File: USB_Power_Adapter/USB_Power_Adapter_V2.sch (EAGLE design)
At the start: 6 parts, among them J1 MICROUSBMICROUSB_THRU, U1 SC189

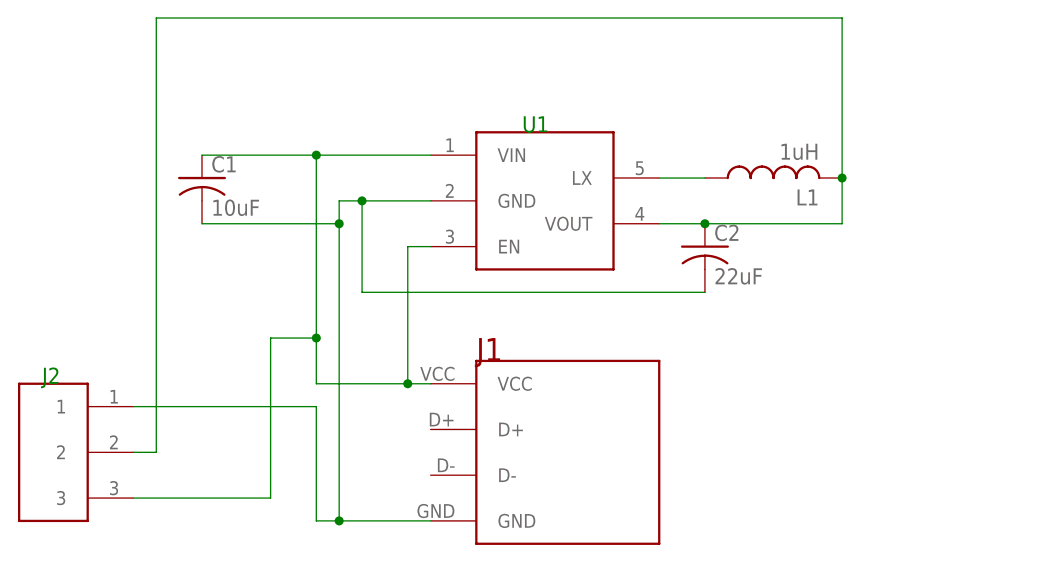
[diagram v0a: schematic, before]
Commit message: Changed spacing and clearance for USB Power Adapter PCB
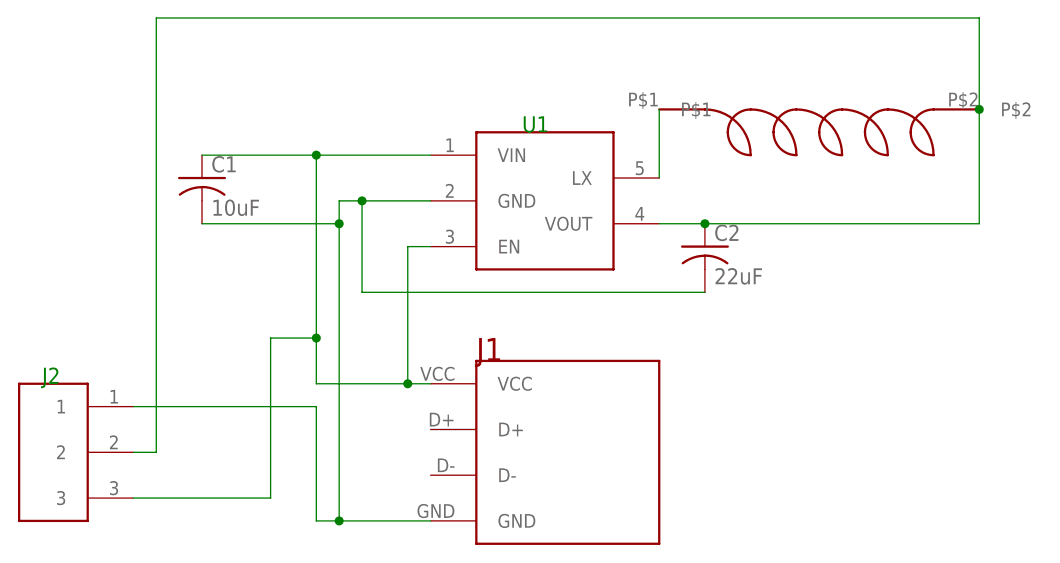
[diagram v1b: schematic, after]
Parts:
- removed L1: 1uH, resistor:L-USL3225M
- added U$1: SMDINDUCTOR, ScottSilver:SMDINDUCTOR
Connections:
- net L: now also U$1.P$1; no longer L1.1
- net VOUT: now also U$1.P$2; no longer L1.2
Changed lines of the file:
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@@
 <part name="C1" library="resistor" deviceset="C-US" device="C0805K" value="10uF"/>
 <part name="C2" library="resistor" deviceset="C-US" device="C0805K" value="22uF"/>
-<part name="L1" library="resistor" deviceset="L-US" device="L3225M" value="1uH"/>
 <part name="U$2" library="ScottSilver" deviceset="DF3_1X3" device=""/>
+<part name="U$1" library="ScottSilver" deviceset="SMDINDUCTOR" device=""/>
 </parts>
 <sheets>
@@
 <instance part="C1" gate="G$1" x="20.32" y="86.36"/>
 <instance part="C2" gate="G$1" x="76.2" y="78.74"/>
-<instance part="L1" gate="G$1" x="83.82" y="86.36" rot="R90"/>
 <instance part="U$2" gate="G$1" x="5.08" y="55.88" rot="MR0"/>
+<instance part="U$1" gate="G$1" x="88.9" y="91.44"/>
 </instances>
 <busses>
@@
 <net name="VOUT" class="0">
 <segment>
-<pinref part="U1" gate="G$1" pin="VOUT"/>
-<pinref part="C2" gate="G$1" pin="1"/>
-<wire x1="71.12" y1="81.28" x2="76.2" y2="81.28" width="0.1524" layer="91"/>
-<pinref part="L1" gate="G$1" pin="2"/>
-<wire x1="91.44" y1="86.36" x2="91.44" y2="81.28" width="0.1524" layer="91"/>
-<wire x1="91.44" y1="81.28" x2="76.2" y2="81.28" width="0.1524" layer="91"/>
-<wire x1="91.44" y1="86.36" x2="91.44" y2="104.14" width="0.1524" layer="91"/>
-<wire x1="91.44" y1="104.14" x2="15.24" y2="104.14" width="0.1524" layer="91"/>
+<wire x1="106.68" y1="104.14" x2="15.24" y2="104.14" width="0.1524" layer="91"/>
 <wire x1="15.24" y1="104.14" x2="15.24" y2="55.88" width="0.1524" layer="91"/>
 <wire x1="12.7" y1="55.88" x2="15.24" y2="55.88" width="0.1524" layer="91"/>
 <pinref part="U$2" gate="G$1" pin="2"/>
+<pinref part="U$1" gate="G$1" pin="P$2"/>
+<wire x1="106.68" y1="104.14" x2="106.68" y2="93.98" width="0.1524" layer="91"/>
+<pinref part="C2" gate="G$1" pin="1"/>
 <junction x="76.2" y="81.28"/>
-<junction x="91.44" y="86.36"/>
+<pinref part="U1" gate="G$1" pin="VOUT"/>
+<wire x1="71.12" y1="81.28" x2="76.2" y2="81.28" width="0.1524" layer="91"/>
+<wire x1="106.68" y1="93.98" x2="106.68" y2="81.28" width="0.1524" layer="91"/>
+<wire x1="106.68" y1="81.28" x2="76.2" y2="81.28" width="0.1524" layer="91"/>
+<junction x="106.68" y="93.98"/>
 </segment>
 </net>
@@
 <segment>
 <pinref part="U1" gate="G$1" pin="LX"/>
-<pinref part="L1" gate="G$1" pin="1"/>
-<wire x1="76.2" y1="86.36" x2="71.12" y2="86.36" width="0.1524" layer="91"/>
+<wire x1="71.12" y1="93.98" x2="71.12" y2="86.36" width="0.1524" layer="91"/>
+<pinref part="U$1" gate="G$1" pin="P$1"/>
 </segment>
 </net>
